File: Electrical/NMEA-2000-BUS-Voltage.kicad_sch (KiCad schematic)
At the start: 13 parts, among them J1 Conn_01x07, J2 Conn_01x02, SW1 SW_Push, U1 WeMos_D1_mini, U2 LM7805_TO220

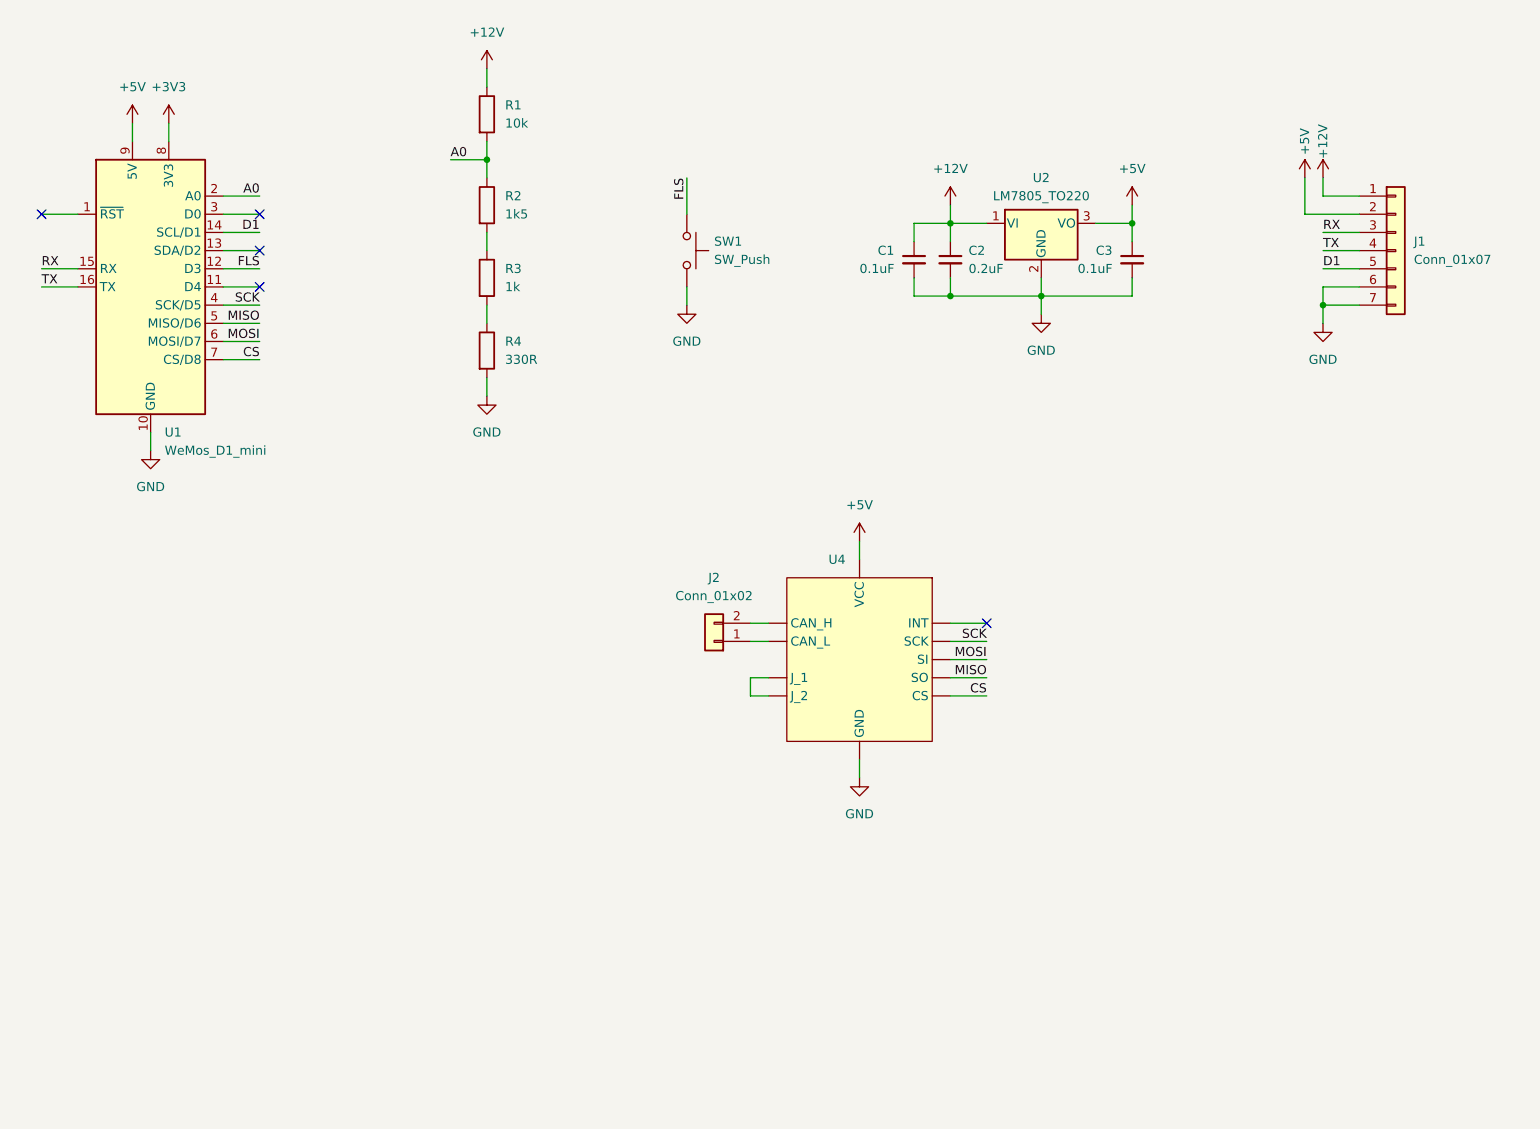
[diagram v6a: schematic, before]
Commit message: Removed MCP2515
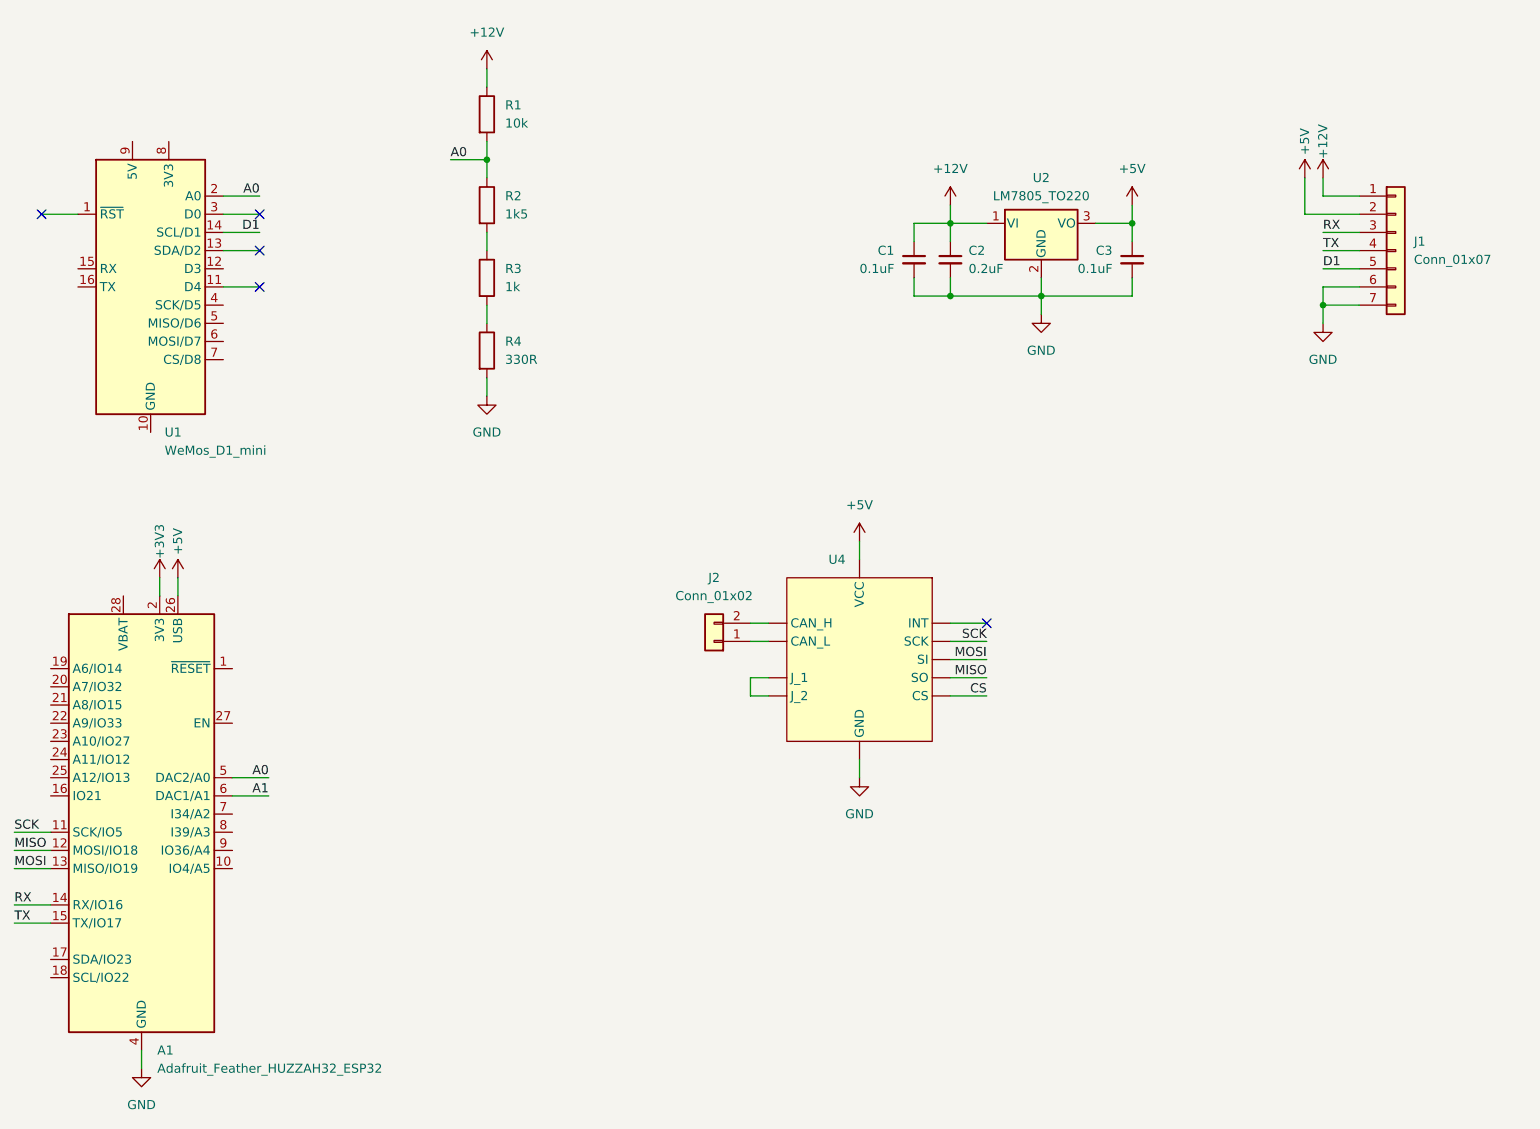
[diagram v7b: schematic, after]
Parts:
- removed SW1: SW_Push, symbol Switch:SW_Push
- added A1: Adafruit_Feather_HUZZAH32_ESP32, Module:Adafruit_Feather, symbol MCU_Module:Adafruit_Feather_HUZZAH32_ESP32
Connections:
- net +3V3: now also A1.2 (3V3); no longer U1.8 (3V3)
- net +5V: now also A1.26 (USB); no longer U1.9 (5V)
- net A0: now also A1.5 (DAC2/A0)
- net CS: no longer U1.7 (CS/D8)
- net GND: now also A1.4 (GND); no longer U1.10 (GND)
- net MISO: now also A1.12 (MOSI/IO18); no longer U1.5 (MISO/D6)
- net MOSI: now also A1.13 (MISO/IO19); no longer U1.6 (MOSI/D7)
- net RX: now also A1.14 (RX/IO16); no longer U1.15 (RX)
- net SCK: now also A1.11 (SCK/IO5); no longer U1.4 (SCK/D5)
- net TX: now also A1.15 (TX/IO17); no longer U1.16 (TX)
- net FLS: no longer names the net of U1.12 (D3)
- new net A1: A1.6 (DAC1/A1)

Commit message: Added SN65HVD230 Module to Schematic
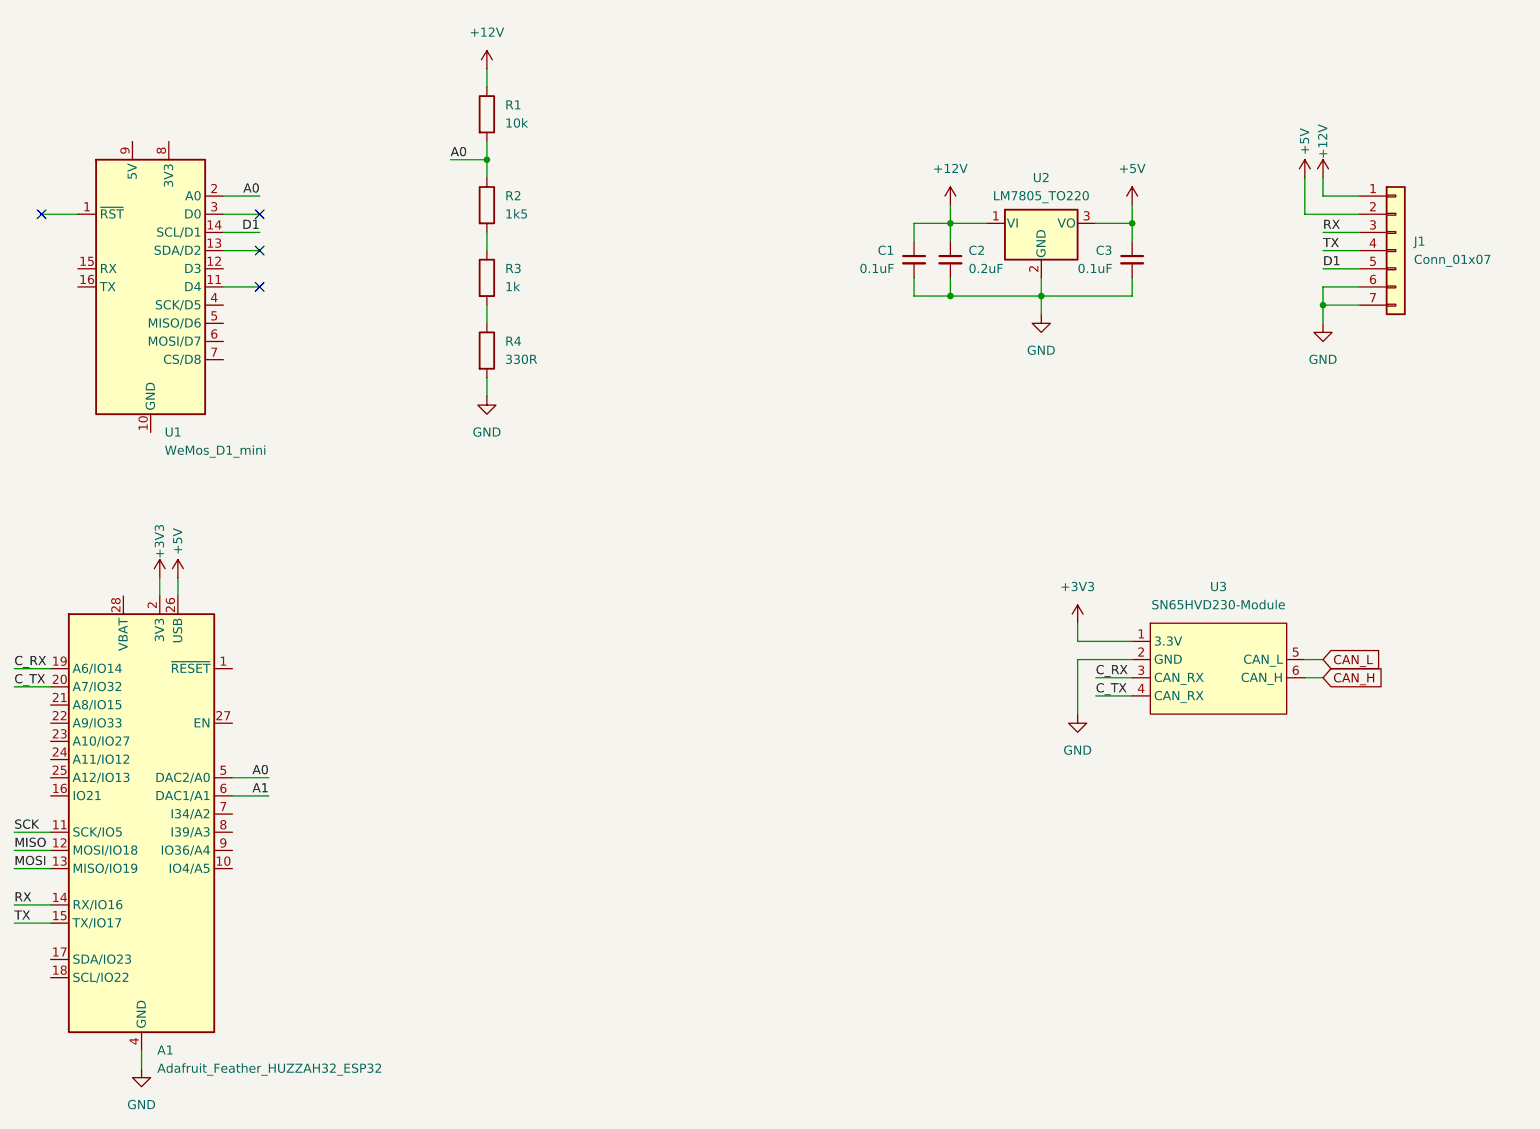
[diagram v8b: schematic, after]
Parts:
- removed J2: Conn_01x02, symbol Connector_Generic:Conn_01x02
- removed U4: ~, symbol Interface_CAN_LIN:MCP2515_Module
- added U3: SN65HVD230-Module, symbol sn65hvd230-module:SN65HVD230-Module
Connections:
- net +3V3: now also U3.1 (3.3V)
- net GND: now also U3.2 (GND)
- net C_RX: now reaches A1.19 (A6/IO14)
- net C_RX: now also U3.3 (CAN_RX)
- net C_TX: now reaches A1.20 (A7/IO32)
- net C_TX: now also U3.4 (CAN_RX)
- new net CAN_H: U3.6 (CAN_H)
- new net CAN_L: U3.5 (CAN_L)
- no-connect marks 5 -> 4
